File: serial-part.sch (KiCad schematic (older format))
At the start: 2 parts, among them P4 serial bus

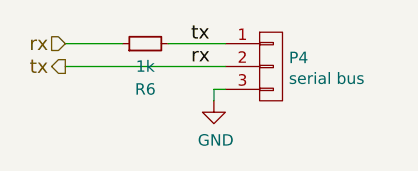
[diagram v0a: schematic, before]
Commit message: schematic seems ok, ongoing routing
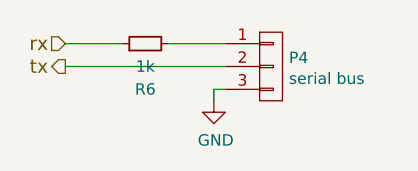
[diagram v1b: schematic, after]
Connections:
- net rx: no longer P4.1 (P1), P4.2 (P2), R6.2
- new net: P4.1 (P1), R6.2
- new net tx: P4.2 (P2)
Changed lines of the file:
@@
 $Descr A4 11693 8268
 encoding utf-8
-Sheet 7 7
+Sheet 7 9
 Title ""
 Date ""
@@
 $EndComp
 $Comp
-L GND #PWR060
+L GND #PWR62
 U 1 1 5702A1E8
 P 5200 2950
-F 0 "#PWR060" H 5200 2700 50  0001 C CNN
+F 0 "#PWR62" H 5200 2700 50  0001 C CNN
 F 1 "GND" H 5208 2777 50  0000 C CNN
 F 2 "" H 5200 2950 50  0000 C CNN
@@
 Wire Wire Line
 	5200 2900 5250 2900
-Text Label 5100 2700 0    60   ~ 0
-tx
-Text Label 5100 2800 0    60   ~ 0
-rx
 Wire Wire Line
 	4550 2800 5250 2800
